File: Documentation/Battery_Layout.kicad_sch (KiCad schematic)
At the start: 43 parts, among them K4 AIR 1 GV200, K5 AIR 2 GV200, U1 UD, U10 UD, U11 UD, U12 UD, U13 UD, U14 UD, U15 UD, U16 UD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

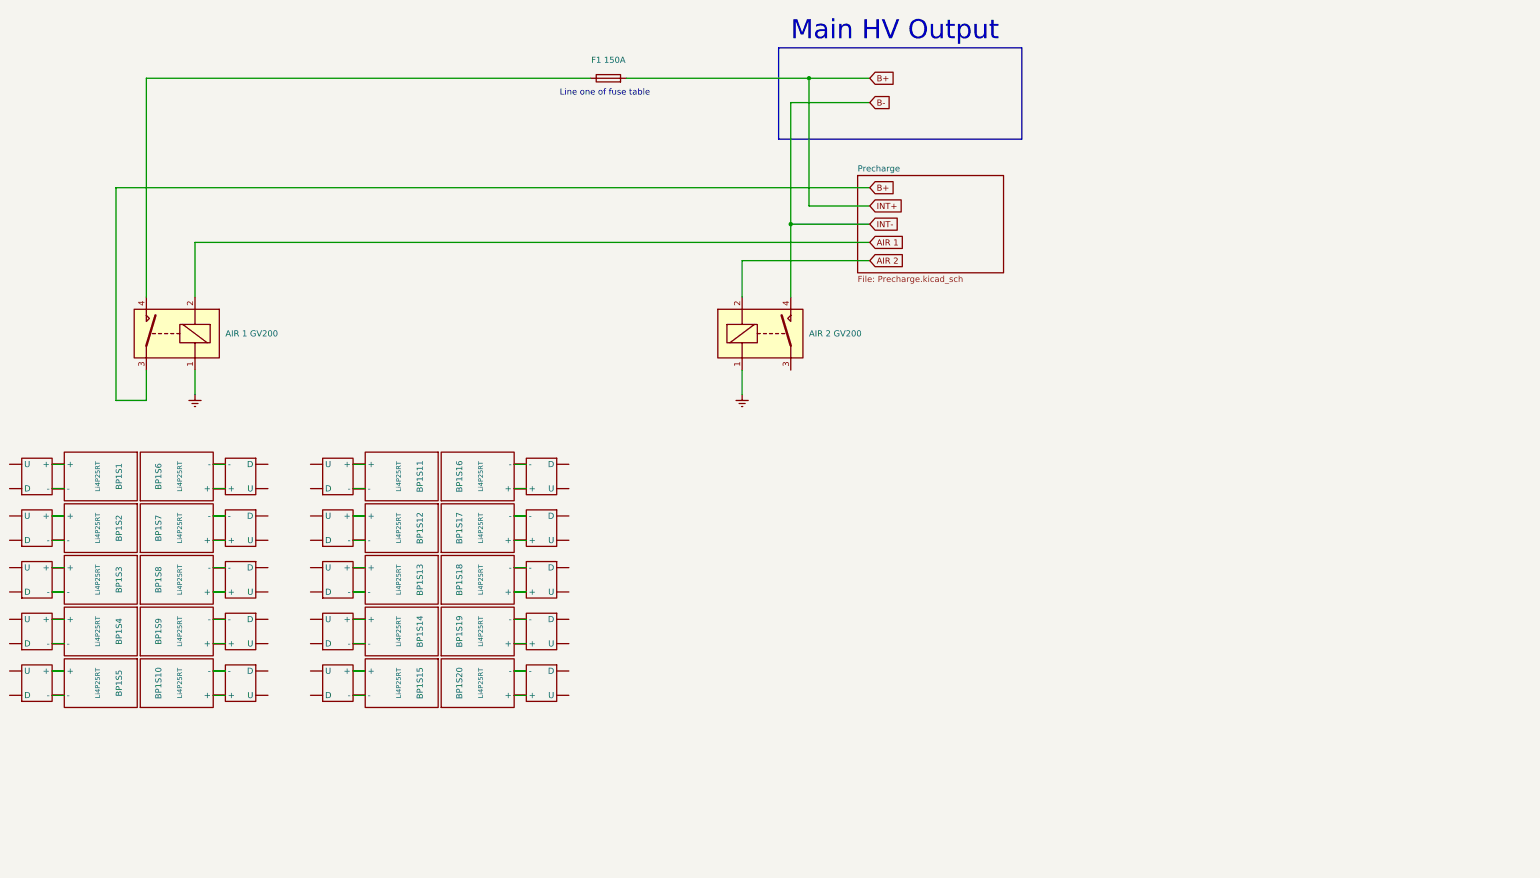
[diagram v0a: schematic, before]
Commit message: finished battery schematic and saftey loop
finished battery schematic and saftey loop
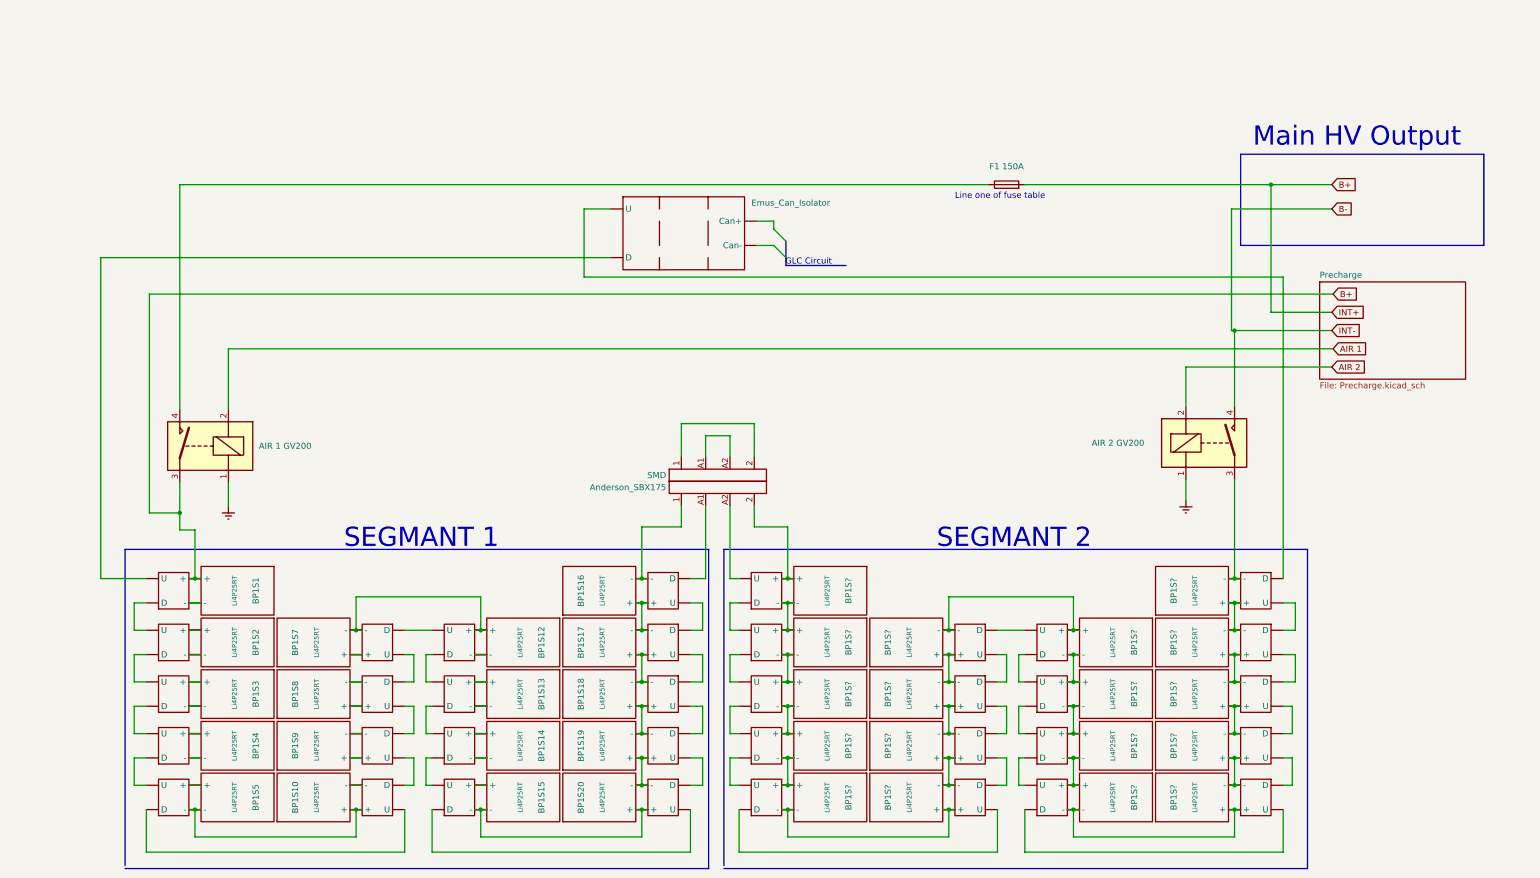
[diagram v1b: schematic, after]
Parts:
- removed BP1S11, BP1S6: Li4P25RT, symbol AERO_Symbols:Li4P25RT
- removed U11, U6: UD, symbol AERO_Symbols:UD
- added BP1S? (x18): Li4P25RT, symbol AERO_Symbols:Li4P25RT
- added SMD: Anderson_SBX175, symbol AERO_Symbols:Anderson_SBX175
- added U? (x18): UD, symbol AERO_Symbols:UD
- added c?: Emus_Can_Isolator, symbol AERO_Symbols:Emus_Can_Isolator
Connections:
- net B+: now also BP1S1. (-), U1. (U)
- net at U5. (U): now also U10. (U)
- net at BP1S5. (-), U5. (U): now also BP1S10. (-), U10. (U)
- net at U4. (U): now also BP1S4. (-)
- net at U13. (U): now also U12. (U)
- net at BP1S16. (-), U16. (U): now also BP1S17. (-), U17. (U)
- net at U16. (U): now also U17. (U); no longer BP1S16. (-)
- net at U15. (U): now also U20. (U)
- net at BP1S15. (-), U15. (U): now also BP1S20. (-), U20. (U)
- net at U14. (U): now also BP1S14. (-)
- net at U2. (U): now also BP1S2. (-)
- net at U18. (U): now also U19. (U)
- net at BP1S18. (-), U18. (U): now also BP1S17. (-), U17. (U)
- net at U9. (U): now also U8. (U); no longer BP1S9. (-)
- net at U10. (U): now also U9. (U); no longer BP1S10. (-)
- net at U20. (U): now also U19. (U)
- net at BP1S20. (-), U20. (U): now also BP1S19. (-), U19. (U)
- net at U8. (U): now also U7. (U); no longer BP1S8. (-)
- net at BP1S7. (-), U7. (U): now also BP1S12. (-), U12. (U)
- net at U7. (U): now also U12. (U); no longer BP1S7. (-)
- net at U17. (U): now also U18. (U)
- net at K5.3: now also BP1S?. (-), U?. (U)
- net at U12. (U): now also BP1S12. (-)
- new net: BP1S1. (-), U1. (U)
- new net: U1. (U), U2. (U)
- new net: U1. (U), c?. (U)
- new net: U4. (U), U5. (U)
- new net: BP1S5. (-), U5. (U)
- new net: BP1S?. (-), BP1S?. (-), U?. (U), U?. (U) (x17)
- new net: U3. (U), U4. (U)
- new net: BP1S4. (-), U4. (U)
- new net: U13. (U), U14. (U)
- new net: BP1S13. (-), U13. (U)
- new net: BP1S16. (-), SMD.1, U16. (U)
- new net: U14. (U), U15. (U)
- new net: BP1S15. (-), U15. (U)
- new net: BP1S14. (-), U14. (U)
- new net: U2. (U), U3. (U)
- new net: BP1S2. (-), U2. (U)
- new net: U?. (U), U?. (U) (x17)
- new net: SMD.A1, U16. (U)
- new net: U?. (U), c?. (U)
- new net: BP1S18. (-), BP1S19. (-), U18. (U), U19. (U)
- new net: BP1S9. (-), U9. (U)
- new net: BP1S?. (-), SMD.2, U?. (U)
- new net: BP1S3. (-), U3. (U)
- new net: SMD.1, SMD.2
- new net: SMD.A1, SMD.A2
- new net: SMD.A2, U?. (U)
- new net: BP1S8. (-), U8. (U)
- new net: BP1S7. (-), U7. (U)
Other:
- note added: "GLC Circuit"
- note added: "SEGMANT 1"
- note added: "SEGMANT 2"
- moved on the sheet: BP1S1, BP1S10, BP1S12, BP1S13, BP1S14, BP1S15, BP1S16, BP1S17, BP1S18, BP1S19, BP1S2, BP1S20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
